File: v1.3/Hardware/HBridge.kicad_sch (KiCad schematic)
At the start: 49 parts, among them J10 DG25C-B-04P-13-00AH, J3 DG25C-B-03P-13-00AH, Q1 IXGH48N60C3D1, Q2 IXGH48N60C3D1, Q23 MMBT3904, Q24 MMBT3904, U8 HCPL-3120, U9 HCPL-3120

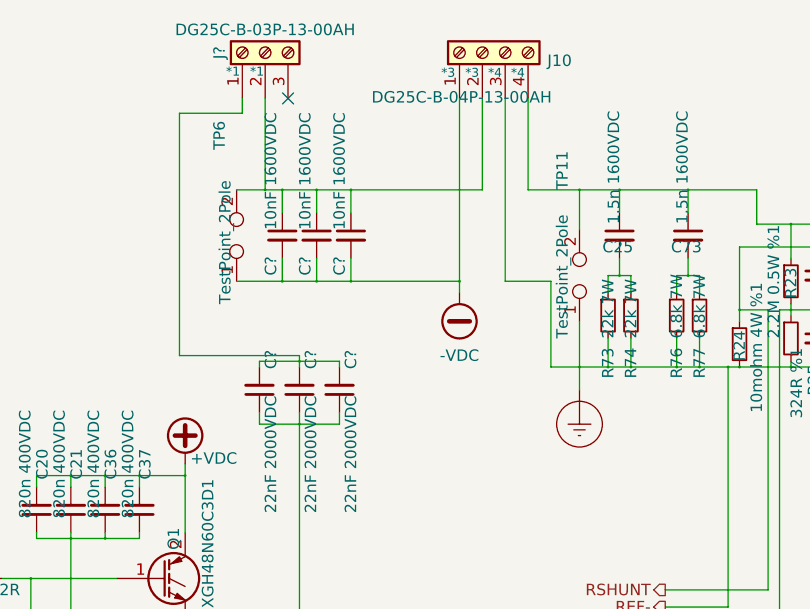
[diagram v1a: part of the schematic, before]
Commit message: v1.3 Schematic, footprints and BOM updated.
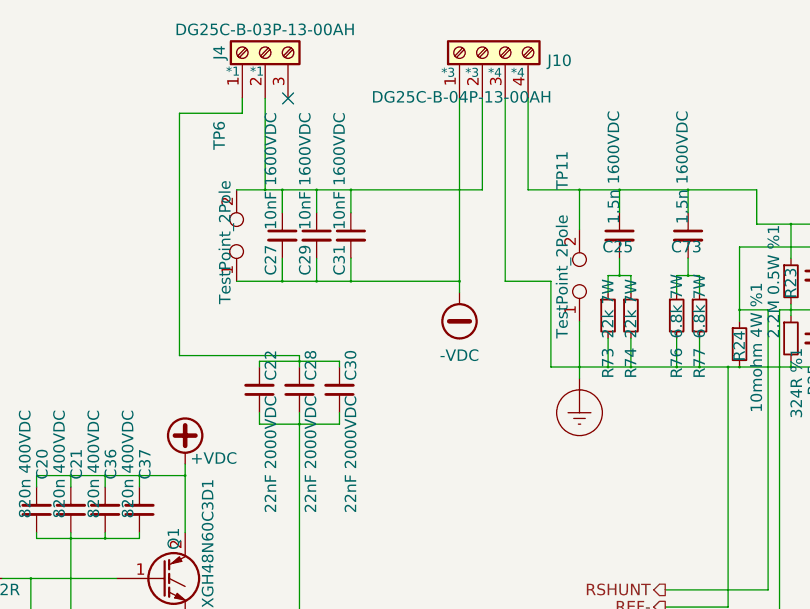
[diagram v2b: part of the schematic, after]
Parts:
- C22, C28, C30: renamed from C?; footprint (none) -> Capacitor_THT:C_Rect_L26.5mm_W10.5mm_P22.50mm_MKS4
- C27, C29, C31: renamed from C?; footprint (none) -> Capacitor_THT:C_Rect_L18.0mm_W6.0mm_P15.00mm_FKS3_FKP3
- R14, R15: footprint (none) -> Resistor_SMD:R_1206_3216Metric
- gave numbers to parts that had none: 1
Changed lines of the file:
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@@
     (stroke (width 0) (type solid) (color 0 0 0 0))
   )
-  (wire (pts (xy 175.895 59.055) (xy 175.895 61.595))
+  (wire (pts (xy 175.895 59.055) (xy 175.895 60.325))
     (stroke (width 0) (type solid) (color 0 0 0 0))
   )
@@
   (symbol (lib_id "power:VDD") (at 52.07 93.345 0) (unit 1)
     (in_bom yes) (on_board yes)
-    (property "Reference" "#PWR?" (id 0) (at 52.07 97.155 0)
+    (property "Reference" "#PWR06" (id 0) (at 52.07 97.155 0)
       (effects (font (size 1.27 1.27)) hide)
     )
@@
   (symbol (lib_id "power:VDD") (at 55.245 73.025 0) (unit 1)
     (in_bom yes) (on_board yes)
-    (property "Reference" "#PWR?" (id 0) (at 55.245 76.835 0)
+    (property "Reference" "#PWR07" (id 0) (at 55.245 76.835 0)
       (effects (font (size 1.27 1.27)) hide)
     )
@@
     (property "Reference" "R14" (id 0) (at 106.68 83.82 90))
     (property "Value" "8.2R" (id 1) (at 111.76 83.82 90))
-    (property "Footprint" "" (id 2) (at 109.22 82.55 0)
+    (property "Footprint" "Resistor_SMD:R_1206_3216Metric" (id 2) (at 109.22 82.55 0)
       (effects (font (size 1.27 1.27)) hide)
     )
@@
     (property "Reference" "R15" (id 0) (at 106.045 104.775 90))
     (property "Value" "8.2R" (id 1) (at 111.125 104.775 90))
-    (property "Footprint" "" (id 2) (at 109.22 103.505 0)
+    (property "Footprint" "Resistor_SMD:R_1206_3216Metric" (id 2) (at 109.22 103.505 0)
       (effects (font (size 1.27 1.27)) hide)
     )
@@
   (symbol (lib_name "Device:C_Small_10") (lib_id "Device:C_Small") (at 140.335 61.595 180) (unit 1)
     (in_bom yes) (on_board yes)
-    (property "Reference" "C?" (id 0) (at 141.605 57.15 90)
+    (property "Reference" "C22" (id 0) (at 141.605 57.15 90)
       (effects (font (size 1.27 1.27)) (justify left))
     )
@@
       (effects (font (size 1.27 1.27)) (justify left))
     )
-    (property "Footprint" "" (id 2) (at 140.335 61.595 0)
+    (property "Footprint" "Capacitor_THT:C_Rect_L26.5mm_W10.5mm_P22.50mm_MKS4" (id 2) (at 140.335 61.595 0)
       (effects (font (size 1.27 1.27)) hide)
     )
@@
   (symbol (lib_name "Device:C_Small_10") (lib_id "Device:C_Small") (at 142.875 44.45 0) (unit 1)
     (in_bom yes) (on_board yes)
-    (property "Reference" "C?" (id 0) (at 141.605 48.895 90)
+    (property "Reference" "C27" (id 0) (at 141.605 48.895 90)
       (effects (font (size 1.27 1.27)) (justify left))
     )
@@
       (effects (font (size 1.27 1.27)) (justify left))
     )
-    (property "Footprint" "" (id 2) (at 142.875 44.45 0)
+    (property "Footprint" "Capacitor_THT:C_Rect_L18.0mm_W6.0mm_P15.00mm_FKS3_FKP3" (id 2) (at 142.875 44.45 0)
       (effects (font (size 1.27 1.27)) hide)
     )
@@
   (symbol (lib_name "Device:C_Small_10") (lib_id "Device:C_Small") (at 144.78 61.595 180) (unit 1)
     (in_bom yes) (on_board yes)
-    (property "Reference" "C?" (id 0) (at 146.05 57.15 90)
+    (property "Reference" "C28" (id 0) (at 146.05 57.15 90)
       (effects (font (size 1.27 1.27)) (justify left))
     )
@@
       (effects (font (size 1.27 1.27)) (justify left))
     )
-    (property "Footprint" "" (id 2) (at 144.78 61.595 0)
+    (property "Footprint" "Capacitor_THT:C_Rect_L26.5mm_W10.5mm_P22.50mm_MKS4" (id 2) (at 144.78 61.595 0)
       (effects (font (size 1.27 1.27)) hide)
     )
@@
   (symbol (lib_name "Device:C_Small_10") (lib_id "Device:C_Small") (at 146.685 44.45 0) (unit 1)
     (in_bom yes) (on_board yes)
-    (property "Reference" "C?" (id 0) (at 145.415 48.895 90)
+    (property "Reference" "C29" (id 0) (at 145.415 48.895 90)
       (effects (font (size 1.27 1.27)) (justify left))
     )
@@
       (effects (font (size 1.27 1.27)) (justify left))
     )
-    (property "Footprint" "" (id 2) (at 146.685 44.45 0)
+    (property "Footprint" "Capacitor_THT:C_Rect_L18.0mm_W6.0mm_P15.00mm_FKS3_FKP3" (id 2) (at 146.685 44.45 0)
       (effects (font (size 1.27 1.27)) hide)
     )
@@
   (symbol (lib_name "Device:C_Small_10") (lib_id "Device:C_Small") (at 149.225 61.595 180) (unit 1)
     (in_bom yes) (on_board yes)
-    (property "Reference" "C?" (id 0) (at 150.495 57.15 90)
+    (property "Reference" "C30" (id 0) (at 150.495 57.15 90)
       (effects (font (size 1.27 1.27)) (justify left))
     )
@@
       (effects (font (size 1.27 1.27)) (justify left))
     )
-    (property "Footprint" "" (id 2) (at 149.225 61.595 0)
+    (property "Footprint" "Capacitor_THT:C_Rect_L26.5mm_W10.5mm_P22.50mm_MKS4" (id 2) (at 149.225 61.595 0)
       (effects (font (size 1.27 1.27)) hide)
     )
@@
   (symbol (lib_name "Device:C_Small_10") (lib_id "Device:C_Small") (at 150.495 44.45 0) (unit 1)
     (in_bom yes) (on_board yes)
-    (property "Reference" "C?" (id 0) (at 149.225 48.895 90)
+    (property "Reference" "C31" (id 0) (at 149.225 48.895 90)
       (effects (font (size 1.27 1.27)) (justify left))
     )
@@
       (effects (font (size 1.27 1.27)) (justify left))
     )
-    (property "Footprint" "" (id 2) (at 150.495 44.45 0)
+    (property "Footprint" "Capacitor_THT:C_Rect_L18.0mm_W6.0mm_P15.00mm_FKS3_FKP3" (id 2) (at 150.495 44.45 0)
       (effects (font (size 1.27 1.27)) hide)
     )
@@
     )
   )
-  (symbol (lib_id "power:Earth_Protective") (at 175.895 61.595 0) (unit 1)
-    (in_bom yes) (on_board yes)
-    (property "Reference" "#PWR036" (id 0) (at 182.245 67.945 0)
-      (effects (font (size 1.27 1.27)) hide)
-    )
-    (property "Value" "Earth_Protective" (id 1) (at 187.325 65.405 0)
-      (effects (font (size 1.27 1.27)) hide)
-    )
-    (property "Footprint" "" (id 2) (at 175.895 64.135 0)
-      (effects (font (size 1.27 1.27)) hide)
-    )
-    (property "Datasheet" "~" (id 3) (at 175.895 64.135 0)
+  (symbol (lib_name "power:Earth_Protective_1") (lib_id "power:Earth_Protective") (at 175.895 60.325 0) (unit 1)
+    (in_bom yes) (on_board yes)
+    (property "Reference" "#PWR011" (id 0) (at 182.245 66.675 0)
+      (effects (font (size 1.27 1.27)) hide)
+    )
+    (property "Value" "Earth_Protective" (id 1) (at 187.325 64.135 0)
+      (effects (font (size 1.27 1.27)) hide)
+    )
+    (property "Footprint" "" (id 2) (at 175.895 62.865 0)
+      (effects (font (size 1.27 1.27)) hide)
+    )
+    (property "Datasheet" "~" (id 3) (at 175.895 62.865 0)
       (effects (font (size 1.27 1.27)) hide)
     )
@@
   (symbol (lib_name "Connector:Screw_Terminal_01x03_1") (lib_id "Connector:Screw_Terminal_01x03") (at 140.97 24.13 90) (unit 1)
     (in_bom yes) (on_board yes)
-    (property "Reference" "J?" (id 0) (at 135.89 24.13 0))
+    (property "Reference" "J4" (id 0) (at 135.89 24.13 0))
     (property "Value" "DG25C-B-03P-13-00AH" (id 1) (at 140.97 21.59 90))
     (property "Footprint" "oe_connector:DG25C-B-03P-13-00AH" (id 2) (at 140.97 24.13 0)
